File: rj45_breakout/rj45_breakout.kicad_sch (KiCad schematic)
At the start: 15 parts, among them J10 Conn_01x08, J6 RJ45_Shielded, J9 Conn_02x04_Odd_Even

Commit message: add some missing silkscreen
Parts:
- J9: footprint Connector_PinHeader_2.54mm:PinHeader_2x04_P2.54mm_Horizontal -> Connector_IDC:IDC-Header_2x04_P2.54mm_Horizontal
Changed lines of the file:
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@@
       (effects (font (size 1.27 1.27)))
     )
-    (property "Footprint" "Connector_PinHeader_2.54mm:PinHeader_2x04_P2.54mm_Horizontal" (at 205.105 74.295 0)
+    (property "Footprint" "Connector_IDC:IDC-Header_2x04_P2.54mm_Horizontal" (at 205.105 74.295 0)
       (effects (font (size 1.27 1.27)) hide)
     )

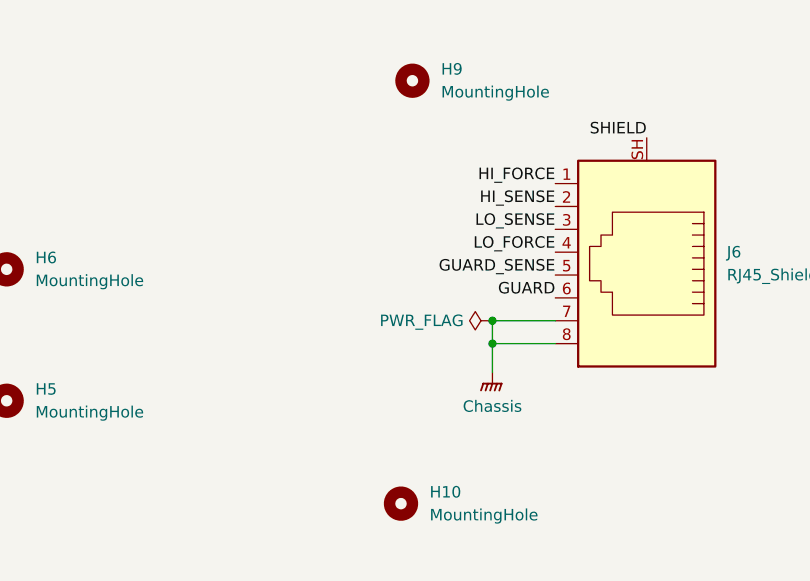
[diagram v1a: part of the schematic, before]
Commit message: fix up rj45 pad numbering
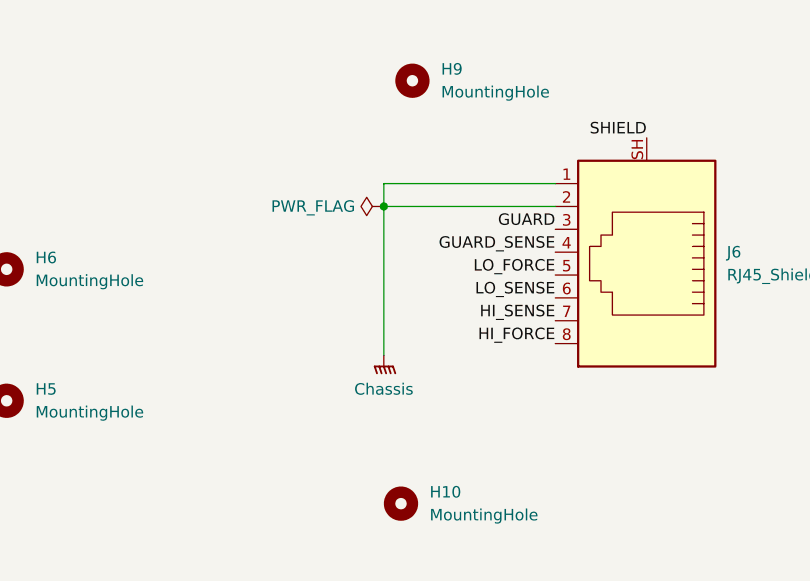
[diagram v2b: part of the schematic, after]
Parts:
- J6: footprint custom_footprints:RJ45_WURTH_615008142621_horizontal_shield -> custom_footprints:RJ45_WURTH_615008142621
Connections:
- net GNDPWR: now also J6.1, J6.2; no longer J6.7, J6.8
- net GUARD: now also J6.3; no longer J6.6
- net GUARD_SENSE: now also J6.4; no longer J6.5
- net HI_FORCE: now also J6.8; no longer J6.1
- net HI_SENSE: now also J6.7; no longer J6.2
- net LO_FORCE: now also J6.5; no longer J6.4
- net LO_SENSE: now also J6.6; no longer J6.3
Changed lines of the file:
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@@
 (kicad_sch (version 20230121) (generator eeschema)
   (paper "A4")
-  (junction (at 131.445 86.36) (diameter 0) (color 0 0 0 0)
-  )
-  (junction (at 131.445 83.82) (diameter 0) (color 0 0 0 0)
+  (junction (at 119.38 71.12) (diameter 0) (color 0 0 0 0)
+  )
+  (wire (pts (xy 119.38 68.58) (xy 119.38 71.12))
+    (stroke (width 0) (type default))
   )
   (wire (pts (xy 203.2 112.395) (xy 207.01 112.395))
     (stroke (width 0) (type default))
   )
-  (wire (pts (xy 138.43 83.82) (xy 131.445 83.82))
-    (stroke (width 0) (type default))
-  )
-  (wire (pts (xy 131.445 83.82) (xy 131.445 86.36))
-    (stroke (width 0) (type default))
-  )
-  (wire (pts (xy 138.43 86.36) (xy 131.445 86.36))
+  (wire (pts (xy 138.43 68.58) (xy 119.38 68.58))
+    (stroke (width 0) (type default))
+  )
+  (wire (pts (xy 119.38 71.12) (xy 119.38 87.63))
     (stroke (width 0) (type default))
   )
@@
     (stroke (width 0) (type default))
   )
-  (wire (pts (xy 131.445 86.36) (xy 131.445 89.535))
-    (stroke (width 0) (type default))
-  )
-  (label "GUARD_SENSE" (at 138.43 78.74 180) (fields_autoplaced)
-    (effects (font (size 1.27 1.27)) (justify right bottom))
-  )
-  (label "GUARD" (at 138.43 81.28 180) (fields_autoplaced)
+  (wire (pts (xy 119.38 71.12) (xy 138.43 71.12))
+    (stroke (width 0) (type default))
+  )
+  (label "GUARD_SENSE" (at 138.43 76.2 180) (fields_autoplaced)
+    (effects (font (size 1.27 1.27)) (justify right bottom))
+  )
+  (label "GUARD" (at 138.43 73.66 180) (fields_autoplaced)
     (effects (font (size 1.27 1.27)) (justify right bottom))
   )
@@
     (effects (font (size 1.27 1.27)) (justify right bottom))
   )
-  (label "LO_SENSE" (at 138.43 73.66 180) (fields_autoplaced)
-    (effects (font (size 1.27 1.27)) (justify right bottom))
-  )
-  (label "HI_FORCE" (at 138.43 68.58 180) (fields_autoplaced)
-    (effects (font (size 1.27 1.27)) (justify right bottom))
-  )
-  (label "HI_SENSE" (at 138.43 71.12 180) (fields_autoplaced)
+  (label "LO_SENSE" (at 138.43 81.28 180) (fields_autoplaced)
+    (effects (font (size 1.27 1.27)) (justify right bottom))
+  )
+  (label "HI_FORCE" (at 138.43 86.36 180) (fields_autoplaced)
+    (effects (font (size 1.27 1.27)) (justify right bottom))
+  )
+  (label "HI_SENSE" (at 138.43 83.82 180) (fields_autoplaced)
     (effects (font (size 1.27 1.27)) (justify right bottom))
   )
@@
     (effects (font (size 1.27 1.27)) (justify right bottom))
   )
-  (label "LO_FORCE" (at 138.43 76.2 180) (fields_autoplaced)
+  (label "LO_FORCE" (at 138.43 78.74 180) (fields_autoplaced)
     (effects (font (size 1.27 1.27)) (justify right bottom))
   )
@@
     )
   )
-  (symbol (lib_id "power:PWR_FLAG") (at 131.445 83.82 90) (unit 1)
-    (in_bom yes) (on_board yes) (dnp no) (fields_autoplaced)
-    (property "Reference" "#FLG01" (at 129.54 83.82 0)
-      (effects (font (size 1.27 1.27)) hide)
-    )
-    (property "Value" "PWR_FLAG" (at 128.27 83.8199 90)
-      (effects (font (size 1.27 1.27)) (justify left))
-    )
-    (property "Footprint" "" (at 131.445 83.82 0)
-      (effects (font (size 1.27 1.27)) hide)
-    )
-    (property "Datasheet" "~" (at 131.445 83.82 0)
+  (symbol (lib_id "power:PWR_FLAG") (at 119.38 71.12 90) (mirror x) (unit 1)
+    (in_bom yes) (on_board yes) (dnp no) (fields_autoplaced)
+    (property "Reference" "#FLG01" (at 117.475 71.12 0)
+      (effects (font (size 1.27 1.27)) hide)
+    )
+    (property "Value" "PWR_FLAG" (at 116.205 71.1201 90)
+      (effects (font (size 1.27 1.27)) (justify left))
+    )
+    (property "Footprint" "" (at 119.38 71.12 0)
+      (effects (font (size 1.27 1.27)) hide)
+    )
+    (property "Datasheet" "~" (at 119.38 71.12 0)
       (effects (font (size 1.27 1.27)) hide)
     )
@@
       (effects (font (size 1.27 1.27)) (justify right))
     )
-    (property "Footprint" "custom_footprints:RJ45_WURTH_615008142621_horizontal_shield" (at 148.59 76.835 90)
+    (property "Footprint" "custom_footprints:RJ45_WURTH_615008142621" (at 148.59 76.835 90)
       (effects (font (size 1.27 1.27)) hide)
     )
@@
     )
   )
-  (symbol (lib_id "power:GNDPWR") (at 131.445 89.535 0) (unit 1)
+  (symbol (lib_id "power:GNDPWR") (at 119.38 87.63 0) (mirror y) (unit 1)
     (in_bom yes) (on_board yes) (dnp no)
-    (property "Reference" "#PWR01" (at 131.445 94.615 0)
-      (effects (font (size 1.27 1.27)) hide)
-    )
-    (property "Value" "GNDPWR" (at 131.318 94.615 0)
-      (effects (font (size 1.27 1.27)) hide)
-    )
-    (property "Footprint" "" (at 131.445 90.805 0)
-      (effects (font (size 1.27 1.27)) hide)
-    )
-    (property "Datasheet" "" (at 131.445 90.805 0)
-      (effects (font (size 1.27 1.27)) hide)
-    )
-    (property "label" "Chassis" (at 131.445 93.345 0)
+    (property "Reference" "#PWR01" (at 119.38 92.71 0)
+      (effects (font (size 1.27 1.27)) hide)
+    )
+    (property "Value" "GNDPWR" (at 119.507 92.71 0)
+      (effects (font (size 1.27 1.27)) hide)
+    )
+    (property "Footprint" "" (at 119.38 88.9 0)
+      (effects (font (size 1.27 1.27)) hide)
+    )
+    (property "Datasheet" "" (at 119.38 88.9 0)
+      (effects (font (size 1.27 1.27)) hide)
+    )
+    (property "label" "Chassis" (at 119.38 91.44 0)
       (effects (font (size 1.27 1.27)))
     )

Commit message: shrink steps, add double rj45 to cc
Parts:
- J6: footprint custom_footprints:RJ45_WURTH_615008142621 -> custom_footprints:RJ45_WURTH_61500814221
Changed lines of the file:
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@@
       (effects (font (size 1.27 1.27)) (justify right))
     )
-    (property "Footprint" "custom_footprints:RJ45_WURTH_615008142621" (at 148.59 76.835 90)
+    (property "Footprint" "custom_footprints:RJ45_WURTH_61500814221" (at 148.59 76.835 90)
       (effects (font (size 1.27 1.27)) hide)
     )
